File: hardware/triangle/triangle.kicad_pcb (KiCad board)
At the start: 4 copper layers, 100 x 86.6 mm, 59 parts, among them J1 Conn_01x02_Socket, J2 Conn_01x02_Socket

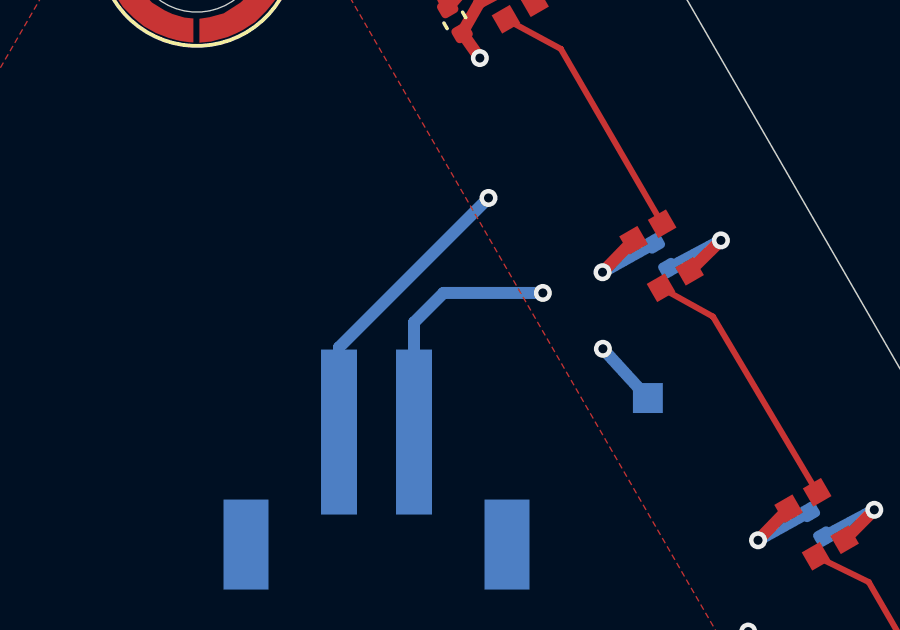
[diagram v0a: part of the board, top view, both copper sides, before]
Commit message: add cap to triangle board and start controller board
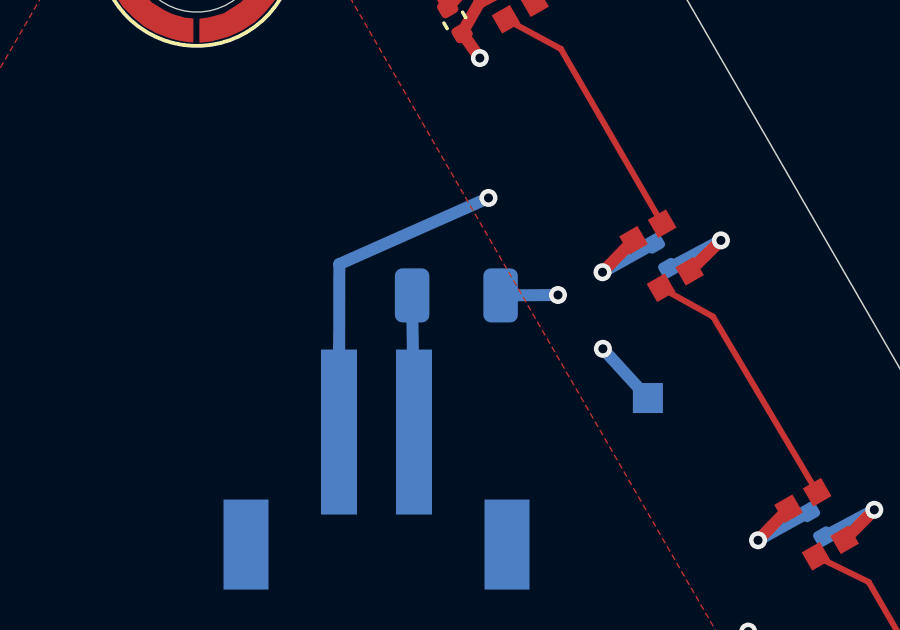
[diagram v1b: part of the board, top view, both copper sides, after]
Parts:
- added C25: 47µF, Capacitor_SMD:C_1206_3216Metric, B.Cu at (158.7, 101.6)
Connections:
- J2 pad 1: 5V Power -> Net-(J2-Pin_1)
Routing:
- net 5V Power: track 106.6 -> 100.2 mm
- net Net-(J2-Pin_1): track 0.00 -> 4.56 mm
- net GND: track 81.9 -> 85.9 mm
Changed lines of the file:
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@@
 		)
 	)
+	(footprint "Capacitor_SMD:C_1206_3216Metric"
+		(layer "B.Cu")
+		(at 158.661541 101.569617 180)
+		(descr "Capacitor SMD 1206 (3216 Metric), square (rectangular) end terminal, IPC-7351 nominal, (Body size source: IPC-SM-782 page 76, https://www.pcb-3d.com/wordpress/wp-content/uploads/ipc-sm-782a_amendment_1_and_2.pdf)")
+		(tags "capacitor")
+		(property "Reference" "C25"
+			(at -0.09265 1.870186 0)
+			(layer "B.SilkS")
+			(effects
+				(font
+					(size 1 1)
+					(thickness 0.15)
+				)
+				(justify mirror)
+			)
+		)
+		(property "Value" "47µF"
+			(at 0 -1.85 0)
+			(layer "B.Fab")
+			(effects
+				(font
+					(size 1 1)
+					(thickness 0.15)
+				)
+				(justify mirror)
+			)
+		)
+		(property "Datasheet" "https://jlc-prod-smt.oss-eu-central-1.aliyuncs.com/smtDataManualFile/8586178840691683328-C77101.pdf?response-content-disposition=attachment%3B%20filename%3DC77101.pdf%3B%20filename%2A%3DUTF-8%27%27C77101.pdf&x-oss-date=20260530T174020Z&x-oss-expires=1800&x-oss-security-token=CAISgAN1q6Ft5B2yfSjIr5n%2Bfdvem%2Bts05SjcVeCpXNkYt5rmo3Mrzz2IHhMdHJsAOodtv0%2FmmhT6PkclqRLcbhpcmfjV%2BZHzLB8qbk31zBO4J7b16cNrbH4M4H6aXeirtuwDsz9SNTCALjPD3nPii50x5bjaDymRCbLGJaViJlhHLN1Ow6jdmhpCctxLAlvo9NgFxm3D%2Fu2NQPwiWf9FVdhvhEG6Vly8qOi2MaRmFy8yFTx0b0SvJ%2BjYMrmPctoN9JnSdC5mfdzau3a1TJ84gRD0a5wkaVA1zbDs5bfISEIuUzebreLqY03dV4mOvdqIcMe8qigz88fk%2FfIioH6xyxKOexoSCnFTOiiupCcQLPyao9jLu6iayqViY7QaIOTqQohZmkAMwVOasAsI3Ngh4zF97Qt0cVNkXO9gWfLI8DtuMleWkppw9R5cnSgc5lCkRRYwGs1287ugXlSQzo890KPDAEovaKCnZ2ZSfh7Y4sNknI6i%2Bfc2Se2MIkIWjBNb6KWD5sagAGr5rmBvHeFC8TZ%2BJcd86gyYT9ErQ9X%2B0arh9aBqEUpMV00uZssw%2BpJ0wDNLR3IfY4Emrombd1Qhrr0MuB3K8fJjJk9FM3xSkdaC6wlZzPtmjTVgp5eXx0QJhMfflRGyQBUK%2FfqX4UcQ0%2FVp31Qo2ufdtTd4b5xoRPi6Re0vJceYCAA&x-oss-signature-version=OSS4-HMAC-SHA256&x-oss-credential=STS.NZK6ajv4MdVHsq3As1nQGuHgM%2F20260530%2Feu-central-1%2Foss%2Faliyun_v4_request&x-oss-signature=60c0d3c6bb64dcbae917457d6a6bcf0bef18835ea05f75f079bc953471331657"
+			(at 0 0 0)
+			(layer "B.Fab")
+			(hide yes)
+			(effects
+				(font
+					(size 1.27 1.27)
+				)
+				(justify mirror)
+			)
+		)
+		(property "Description" "Unpolarized capacitor"
+			(at 0 0 0)
+			(layer "B.Fab")
+			(hide yes)
+			(effects
+				(font
+					(size 1.27 1.27)
+				)
+				(justify mirror)
+			)
+		)
+		(property "KiLib_Generator" "SMD_2terminal_chip_molded"
+			(at 0 0 0)
+			(layer "B.SilkS")
+			(hide yes)
+			(effects
+				(font
+					(size 1 1)
+					(thickness 0.15)
+				)
+				(justify mirror)
+			)
+		)
+		(property "JLCPCB Part #" "C77101"
+			(at 0 0 0)
+			(unlocked yes)
+			(layer "B.Fab")
+			(hide yes)
+			(effects
+				(font
+					(size 1 1)
+					(thickness 0.15)
+				)
+				(justify mirror)
+			)
+		)
+		(property ki_fp_filters "C_*")
+		(sheetname "/")
+		(sheetfile "triangle.kicad_sch")
+		(units
+			(unit
+				(name "A")
+				(pins "1" "2")
+			)
+		)
+		(attr smd)
+		(duplicate_pad_numbers_are_jumpers no)
+		(fp_line
+			(start -0.711252 0.91)
+			(end 0.711252 0.91)
+			(stroke
+				(width 0.12)
+				(type solid)
+			)
+			(layer "B.SilkS")
+		)
+		(fp_line
+			(start -0.711252 -0.91)
+			(end 0.711252 -0.91)
+			(stroke
+				(width 0.12)
+				(type solid)
+			)
+			(layer "B.SilkS")
+		)
+		(fp_rect
+			(start -2.3 1.15)
+			(end 2.3 -1.15)
+			(stroke
+				(width 0.05)
+				(type solid)
+			)
+			(fill no)
+			(layer "B.CrtYd")
+		)
+		(fp_rect
+			(start -1.6 0.8)
+			(end 1.6 -0.8)
+			(stroke
+				(width 0.1)
+				(type solid)
+			)
+			(fill no)
+			(layer "B.Fab")
+		)
+		(fp_text user "${REFERENCE}"
+			(at 0 0 0)
+			(layer "B.Fab")
+			(effects
+				(font
+					(size 0.8 0.8)
+					(thickness 0.12)
+				)
+				(justify mirror)
+			)
+		)
+		(pad "1" smd roundrect
+			(at -1.475 0 180)
+			(size 1.15 1.8)
+			(layers "B.Cu" "B.Mask" "B.Paste")
+			(roundrect_rratio 0.217391)
+			(net "5V Power")
+			(pintype "passive")
+		)
+		(pad "2" smd roundrect
+			(at 1.475 0 180)
+			(size 1.15 1.8)
+			(layers "B.Cu" "B.Mask" "B.Paste")
+			(roundrect_rratio 0.217391)
+			(net "Net-(J2-Pin_1)")
+			(pintype "passive")
+		)
+		(embedded_fonts no)
+		(model "${KICAD10_3DMODEL_DIR}/Capacitor_SMD.3dshapes/C_1206_3216Metric.step"
+			(offset
+				(xyz 0 0 0)
+			)
+			(scale
+				(xyz 1 1 1)
+			)
+			(rotate
+				(xyz 0 0 0)
+			)
+		)
+	)
 	(footprint "TestPoint:TestPoint_Pad_1.0x1.0mm"
 		(layer "B.Cu")
@@
 			(size 1.2 5.5)
 			(layers "B.Cu" "B.Mask" "B.Paste")
-			(net "5V Power")
+			(net "Net-(J2-Pin_1)")
 			(pinfunction "Pin_1_1")
 			(pintype "passive")
@@
 	)
 	(via
-		(at 161.544403 101.488131)
+		(at 162.049594 101.5565)
 		(size 0.6)
 		(drill 0.3)
@@
 	)
 	(segment
-		(start 161.544403 101.488131)
-		(end 158.235421 101.488131)
-		(width 0.4)
-		(layer "B.Cu")
-		(net "5V Power")
-	)
-	(segment
 		(start 170.91 109.614192)
 		(end 172.592834 108.71747)
@@
 	)
 	(segment
-		(start 157.25 102.473552)
-		(end 157.25 106.125)
-		(width 0.4)
-		(layer "B.Cu")
-		(net "5V Power")
-	)
-	(segment
 		(start 159.854704 146.93186)
 		(end 159.854704 145.000296)
@@
 	)
 	(segment
-		(start 158.235421 101.488131)
-		(end 157.25 102.473552)
+		(start 160.136541 101.569617)
+		(end 162.049594 101.5565)
 		(width 0.4)
 		(layer "B.Cu")
@@
 	)
 	(segment
+		(start 154.760897 100.526686)
+		(end 159.732852 98.321599)
+		(width 0.4)
+		(layer "B.Cu")
+		(net "GND")
+	)
+	(segment
 		(start 150.487662 143.115658)
 		(end 150.487662 144.992338)
@@
 	)
 	(segment
-		(start 159.732852 98.321599)
-		(end 154.75 103.304451)
+		(start 154.75 106.125)
+		(end 154.760897 100.526686)
 		(width 0.4)
 		(layer "B.Cu")
@@
 		(net "LED_DATA_OUT")
 	)
+	(segment
+		(start 157.186541 101.569617)
+		(end 157.25 106.125)
+		(width 0.4)
+		(layer "B.Cu")
+		(net "Net-(J2-Pin_1)")
+	)
 	(zone

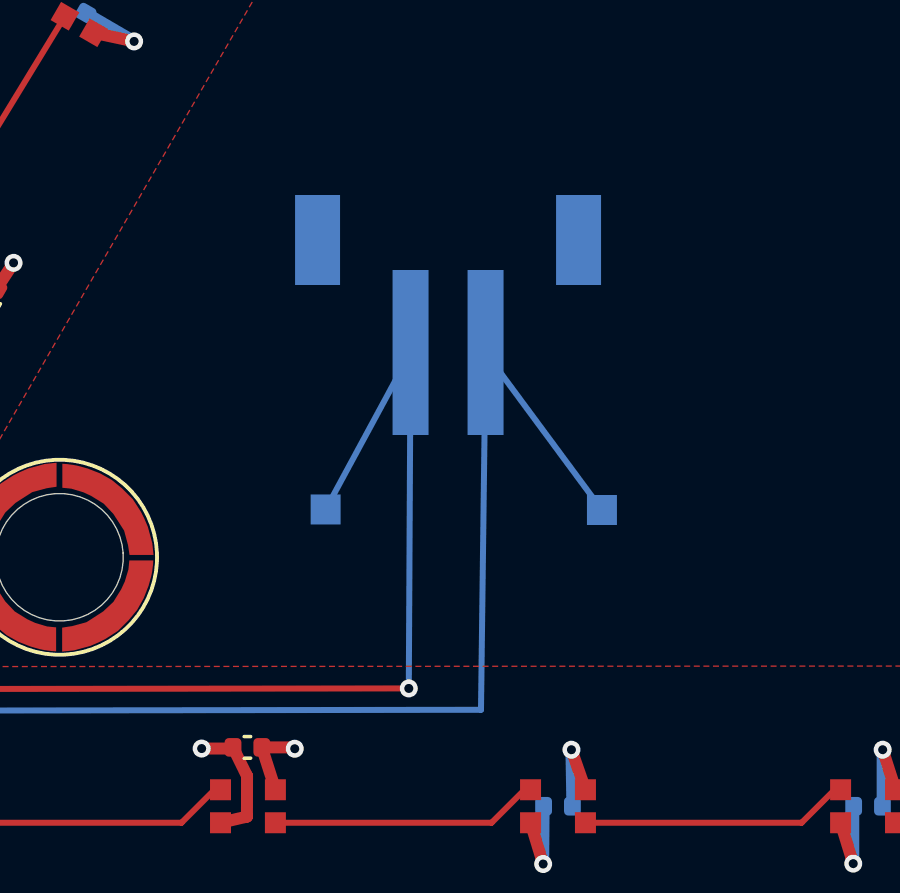
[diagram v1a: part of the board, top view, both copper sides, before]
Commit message: use different socket for data vs power to avoid accidents
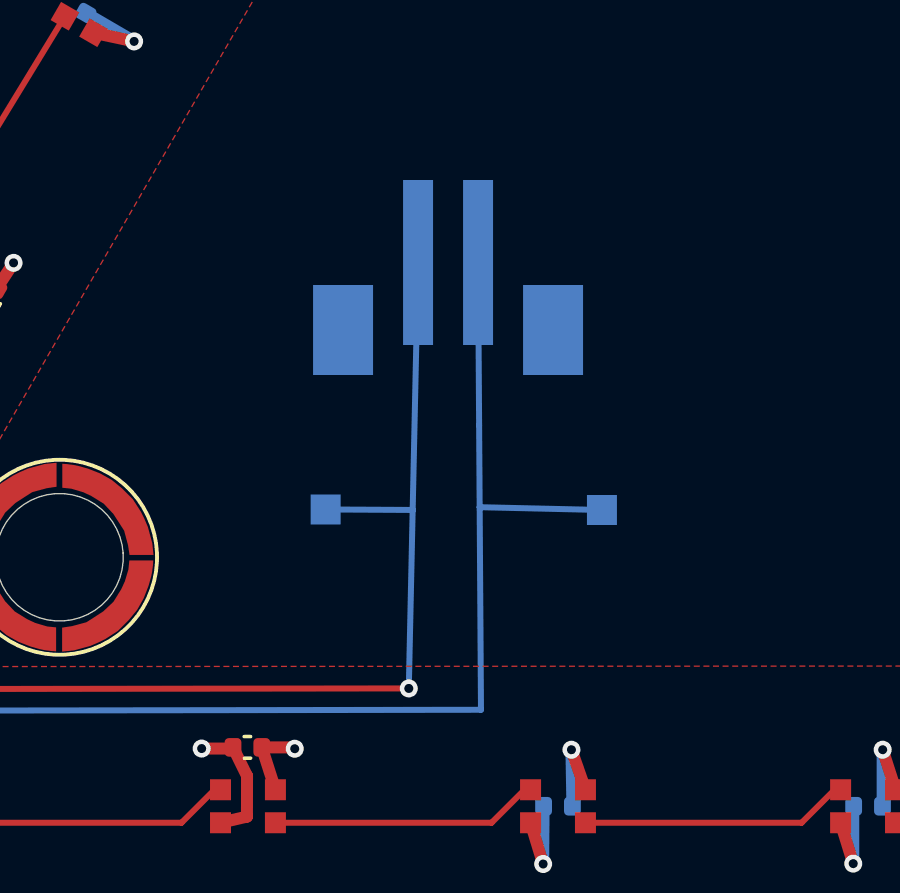
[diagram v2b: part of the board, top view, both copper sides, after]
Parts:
- J1: footprint footprints:CONN-SMD_ZX-XH2.54-2PLT -> footprints:CONN-SMD_B2B-PH-SM4-TBT-LF-SN
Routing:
- net LED_DATA_OUT: track 43.3 -> 43.8 mm
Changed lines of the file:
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@@
 		(embedded_fonts no)
 	)
-	(footprint "footprints:CONN-SMD_ZX-XH2.54-2PLT"
+	(footprint "footprints:CONN-SMD_B2B-PH-SM4-TBT-LF-SN"
 		(layer "B.Cu")
 		(at 136 128)
 		(property "Reference" "J1"
-			(at 0 5.6 180)
+			(at 0 4.6255 180)
 			(layer "B.SilkS")
 			(effects
@@
 		)
 		(property "Value" "Conn_01x02_Socket"
-			(at 0 -5.0255 180)
+			(at 0 -4.85 180)
 			(layer "B.Fab")
 			(effects
@@
 			)
 		)
-		(property "Datasheet" ""
+		(property "Datasheet" "https://jlc-prod-smt.oss-eu-central-1.aliyuncs.com/smtDataManualFile/8588902703158607872-C265003.pdf?response-content-disposition=attachment%3B%20filename%3DC265003.pdf%3B%20filename%2A%3DUTF-8%27%27C265003.pdf&x-oss-date=20260530T184618Z&x-oss-expires=1800&x-oss-security-token=CAISgAN1q6Ft5B2yfSjIr5mMGOPH2b5C56u6RmrwoVgfesNa3pGdrjz2IHhMdHJsAOodtv0%2FmmhT6PkclqRLcbhpcmfjV%2BZHzLB8qYMJrTZO4J7b16cNrbH4M4H6aXeirtuwDsz9SNTCALjPD3nPii50x5bjaDymRCbLGJaViJlhHLN1Ow6jdmhpCctxLAlvo9NgFxm3D%2Fu2NQPwiWf9FVdhvhEG6Vly8qOi2MaRmFy8yFTx0b0SvJ%2BjYMrmPctoN9JnSdC5mfdzau3a1TJ84gRD0a5wkaVA1zbDs5bfISEIuUzebreLqY03dV4mOvdqIcMe8qigz88fk%2FfIioH6xyxKOexoSCnFTOiiupCcQLPyao9jLu6iayqViY7QaIOTqQohZmkAMwVOasAsI3Ngh4zF97Qt0cVNkXO9gWfLI8DtuMleWorMUcNC5tHD0eS19jklBdzSlusJRAJJUVBflCeKEaRNSAd3WGhEfM2%2BBt4QT30w5N2u00S8OSMIj6WwtaKWD5sagAEiB9a8Fe3Xz48X2tP6dxg54Vro9nibq7GRPtzBohN8u1QdmxofnrAafgnnqWIAyQYzEZD7Qmyn521BE9LOYbykf0HEMcjUKnha5PhgCA%2BaTkV%2BbWuE1SITzT9cI0CaBUqZ3vKId6FEL2fcnTSF0BDC6iF%2Bhf1ATGD2uciyP2xLKSAA&x-oss-signature-version=OSS4-HMAC-SHA256&x-oss-credential=STS.NZ9SYs4acPiQDLAEXJvLv1T6L%2F20260530%2Feu-central-1%2Foss%2Faliyun_v4_request&x-oss-signature=9be76bdf4ed042f2478c7de920dfc88ba2fe608f5eef2b87c8aebd4d72e4c4dc"
 			(at 0 0 180)
 			(layer "B.Fab")
@@
 			)
 		)
-		(property "JLCPCB Part #" "C7429680"
+		(property "JLC_3DModel_Q" "17eee4ff8e154fb79314b5fd0affb698"
+			(at 0 0 180)
+			(layer "Cmts.User")
+			(hide yes)
+			(effects
+				(font
+					(size 1.27 1.27)
+				)
+			)
+		)
+		(property "JLC_3D_Size" "8 7"
+			(at 0 0 180)
+			(layer "Cmts.User")
+			(hide yes)
+			(effects
+				(font
+					(size 1.27 1.27)
+				)
+			)
+		)
+		(property "JLCPCB Part #" "C265003"
 			(at 0 0 0)
 			(unlocked yes)
@@
 			)
 		)
-		(attr smd)
 		(duplicate_pad_numbers_are_jumpers no)
 		(fp_line
-			(start -5 -4.025)
-			(end -3.319 -4.025)
-			(stroke
-				(width 0.254)
-				(type default)
-			)
-			(layer "B.SilkS")
-		)
-		(fp_line
-			(start -5 -3.606)
-			(end -5 -4.025)
-			(stroke
-				(width 0.254)
-				(type default)
-			)
-			(layer "B.SilkS")
-		)
-		(fp_line
-			(start -5 1.975)
-			(end -5 -0.144)
+			(start -4 -1.375)
+			(end -1.7315 -1.375)
 			(stroke
 				(width 0.254)
@@
 		)
 		(fp_line
-			(start -5 1.975)
-			(end -2.081 1.975)
+			(start -4 -0.606)
+			(end -4 -1.375)
 			(stroke
 				(width 0.254)
@@
 		)
 		(fp_line
-			(start -3.319 -4.025)
-			(end 3.319 -4.025)
+			(start -4 3.625)
+			(end -4 2.856)
 			(stroke
 				(width 0.254)
@@
 		)
 		(fp_line
-			(start -0.419 1.975)
-			(end 0.419 1.975)
+			(start -4 3.625)
+			(end 4 3.625)
 			(stroke
 				(width 0.254)
@@
 		)
 		(fp_line
-			(start 2.081 1.975)
-			(end 5 1.975)
+			(start -0.269 -1.375)
+			(end 0.2685 -1.375)
 			(stroke
 				(width 0.254)
@@
 		)
 		(fp_line
-			(start 5 -4.025)
-			(end 3.319 -4.025)
+			(start 1.731 -1.375)
+			(end 4 -1.375)
 			(stroke
 				(width 0.254)
@@
 		)
 		(fp_line
-			(start 5 -3.606)
-			(end 5 -4.025)
+			(start 4 -1.375)
+			(end 4 -0.606)
 			(stroke
 				(width 0.254)
@@
 		)
 		(fp_line
-			(start 5 1.975)
-			(end 5 -0.144)
+			(start 4 2.856)
+			(end 4 3.625)
 			(stroke
 				(width 0.254)
@@
 		)
 		(fp_circle
-			(center -2.54 3.148)
-			(end -2.413 3.148)
-			(stroke
-				(width 0.254)
-				(type default)
-			)
-			(fill no)
-			(layer "B.SilkS")
-		)
-		(fp_circle
-			(center -2.54 3.021)
-			(end -2.413 3.021)
+			(center -0.945 -3.066)
+			(end -0.818 -3.066)
 			(stroke
 				(width 0.254)
@@
 		)
 		(fp_rect
-			(start -5.35 4.875)
-			(end 5.35 -4.3005)
+			(start -4.75 3.9005)
+			(end 4.75 -4.125)
 			(stroke
 				(width 0.05)
@@
 		)
 		(fp_line
-			(start -5 -4.025)
-			(end -5 1.975)
+			(start -3.975 -1.375)
+			(end -3.975 3.625)
 			(stroke
 				(width 0.051)
@@
 		)
 		(fp_line
-			(start -5 1.975)
-			(end 5 1.975)
+			(start -3.975 3.625)
+			(end 3.975 3.625)
 			(stroke
 				(width 0.051)
@@
 		)
 		(fp_line
-			(start 5 -4.025)
-			(end -5 -4.025)
+			(start 3.975 -1.375)
+			(end -3.975 -1.375)
 			(stroke
 				(width 0.051)
@@
 		)
 		(fp_line
-			(start 5 1.975)
-			(end 5 -4.025)
+			(start 3.975 3.625)
+			(end 3.975 -1.375)
 			(stroke
 				(width 0.051)
@@
 		(fp_poly
 			(pts
-				(xy -4.944567 4.397961) (xy -4.977039 4.430433) (xy -5.022961 4.430433) (xy -5.055433 4.397961)
-				(xy -5.055433 4.352039) (xy -5.022961 4.319567) (xy -4.977039 4.319567) (xy -4.944567 4.352039)
+				(xy -3.919567 -3.352039) (xy -3.952039 -3.319567) (xy -3.997961 -3.319567) (xy -4.030433 -3.352039)
+				(xy -4.030433 -3.397961) (xy -3.997961 -3.430433) (xy -3.952039 -3.430433) (xy -3.919567 -3.397961)
 			)
 			(stroke
@@
 		(fp_poly
 			(pts
-				(xy -4.85 -0.875) (xy -3.85 -0.875) (xy -3.85 -2.875) (xy -4.85 -2.875)
+				(xy -3.975 2.225) (xy -2.975 2.225) (xy -2.975 0.025) (xy -3.975 0.025)
 			)
 			(stroke
@@
 		(fp_poly
 			(pts
-				(xy -1.57 4.375) (xy -0.93 4.375) (xy -0.93 1.375) (xy -1.57 1.375)
+				(xy -1.25 1.125) (xy -0.75 1.125) (xy -0.75 -3.375) (xy -1.25 -3.375)
 			)
 			(stroke
@@
 		(fp_poly
 			(pts
-				(xy 0.93 4.375) (xy 1.57 4.375) (xy 1.57 1.375) (xy 0.93 1.375)
+				(xy 0.75 1.125) (xy 1.25 1.125) (xy 1.25 -3.375) (xy 0.75 -3.375)
 			)
 			(stroke
@@
 		(fp_poly
 			(pts
-				(xy 3.85 -0.875) (xy 4.85 -0.875) (xy 4.85 -2.875) (xy 3.85 -2.875)
+				(xy 2.975 2.225) (xy 3.975 2.225) (xy 3.975 0.025) (xy 2.975 0.025)
 			)
 			(stroke
@@
 		)
 		(pad "1" smd rect
-			(at -1.25 1.875)
-			(size 1.2 5.5)
+			(at -1 -1.125)
+			(size 1 5.5)
 			(layers "B.Cu" "B.Mask" "B.Paste")
 			(net "LED_DATA_IN")
@@
 		)
 		(pad "2" smd rect
-			(at 1.25 1.875)
-			(size 1.2 5.5)
+			(at 1 -1.125)
+			(size 1 5.5)
 			(layers "B.Cu" "B.Mask" "B.Paste")
 			(net "LED_DATA_OUT")
@@
 		)
 		(pad "3" smd rect
-			(at 4.35 -1.875)
-			(size 1.5 3)
+			(at 3.5 1.125)
+			(size 2 3)
 			(layers "B.Cu" "B.Mask" "B.Paste")
 		)
 		(pad "4" smd rect
-			(at -4.35 -1.875)
-			(size 1.5 3)
+			(at -3.5 1.125)
+			(size 2 3)
 			(layers "B.Cu" "B.Mask" "B.Paste")
 		)
 		(embedded_fonts no)
+		(model "${KIPRJMOD}/EASYEDA_MODELS/CONN-SMD_B2B-PH-SM4-TBT-LF-SN.step"
+			(offset
+				(xyz 0 0.127 0)
+			)
+			(scale
+				(xyz 1 1 1)
+			)
+			(rotate
+				(xyz -0 -0 -0)
+			)
+		)
 	)
 	(footprint "Capacitor_SMD:C_0402_1005Metric"
@@
 	(segment
 		(start 134.691163 141.072204)
-		(end 134.75 129.875)
+		(end 134.820568 135.123484)
 		(width 0.2)
 		(layer "B.Cu")
@@
 	(segment
 		(start 131.919296 135.107303)
-		(end 134.75 129.875)
+		(end 134.820568 135.123484)
+		(width 0.2)
+		(layer "B.Cu")
+		(net "LED_DATA_IN")
+	)
+	(segment
+		(start 134.820568 135.123484)
+		(end 135 126.875)
 		(width 0.2)
 		(layer "B.Cu")
@@
 	)
 	(segment
-		(start 137.25 129.875)
-		(end 141.129437 135.124832)
+		(start 137.097739 141.78407)
+		(end 137.053472 135.031567)
 		(width 0.2)
 		(layer "B.Cu")
@@
 	)
 	(segment
-		(start 137.097739 141.78407)
-		(end 137.25 129.875)
+		(start 137.053472 135.031567)
+		(end 137.035595 132.304688)
 		(width 0.2)
 		(layer "B.Cu")
@@
 	)
 	(segment
+		(start 141.129437 135.124832)
+		(end 137.053472 135.031567)
+		(width 0.2)
+		(layer "B.Cu")
+		(net "LED_DATA_OUT")
+	)
+	(segment
 		(start 114.240491 139.332163)
 		(end 117.970631 141.813173)
 		(width 0.2)
 		(layer "B.Cu")
+		(net "LED_DATA_OUT")
+	)
+	(segment
+		(start 137.035595 132.304688)
+		(end 137 126.875)
+		(width 0.2)
+		(layer "B.Cu")
